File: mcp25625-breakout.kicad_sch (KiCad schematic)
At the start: 9 parts

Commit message: Apply KiCad6 lib
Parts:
- SW1: symbol my-kicad-symbols:SW_Slide_with_cover -> asukiaaa-kicad-symbols:SW_Slide_with_cover
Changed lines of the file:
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@@
     (pin "9")
   )
-  (symbol (lib_id "my-kicad-symbols:SW_Slide_with_cover") (at 168.91 63.5 0) (mirror y) (unit 1)
+  (symbol (lib_id "asukiaaa-kicad-symbols:SW_Slide_with_cover") (at 168.91 63.5 0) (mirror y) (unit 1)
     (in_bom yes) (on_board yes)
     (property "Reference" "SW1" (id 0) (at 168.91 56.261 0))
@@
     )
     (path "/00000000-0000-0000-0000-000060a42d68"
-      (reference "J1") (unit 1) (value "Conn_01x11") (footprint "my-kicad-footprints:PinHeader_1x11_P2.54mm_Vertical_witout_silk")
+      (reference "J1") (unit 1) (value "Conn_01x11") (footprint "asukiaaa-kicad-footprints:PinHeader_1x11_P2.54mm_Vertical_witout_silk")
     )
     (path "/00000000-0000-0000-0000-00006097b02f"
@@
     )
     (path "/00000000-0000-0000-0000-000060bd7c69"
-      (reference "SW1") (unit 1) (value "SW_Slide_with_cover") (footprint "my-kicad-footprints:slide_switch_smd")
+      (reference "SW1") (unit 1) (value "SW_Slide_with_cover") (footprint "asukiaaa-kicad-footprints:slide_switch_smd")
     )
     (path "/00000000-0000-0000-0000-000060968f8d"

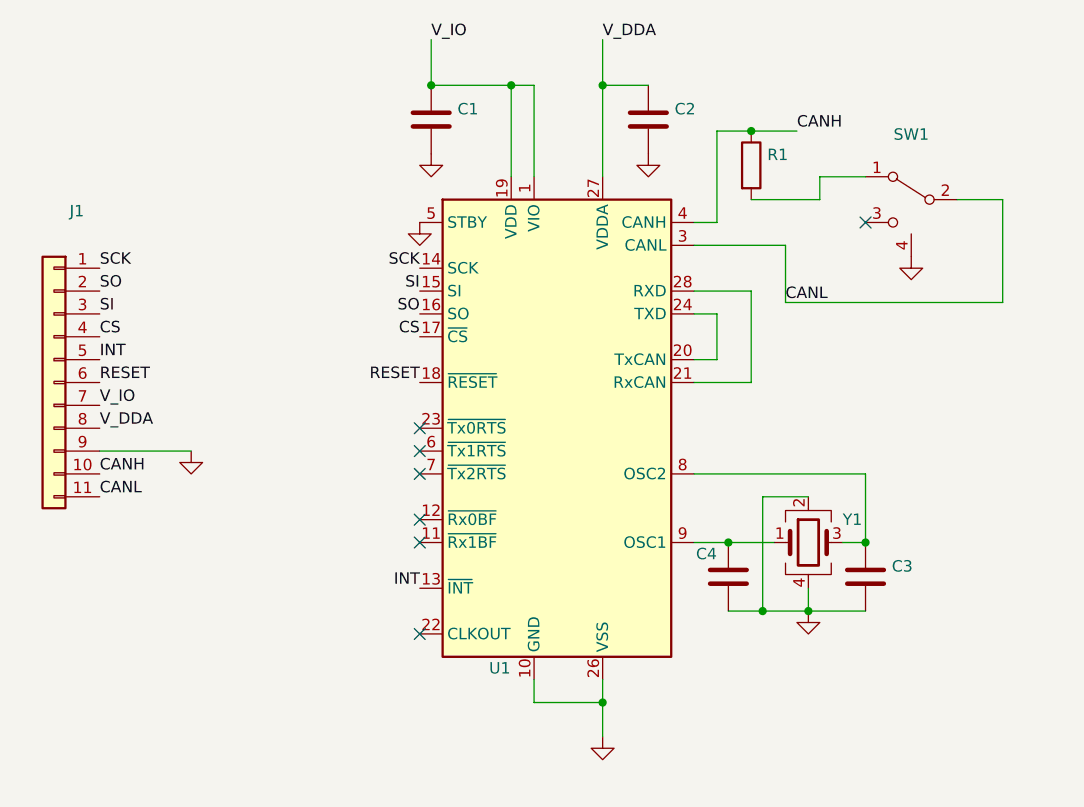
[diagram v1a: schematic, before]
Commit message: Change to not hand solder pad for crystal
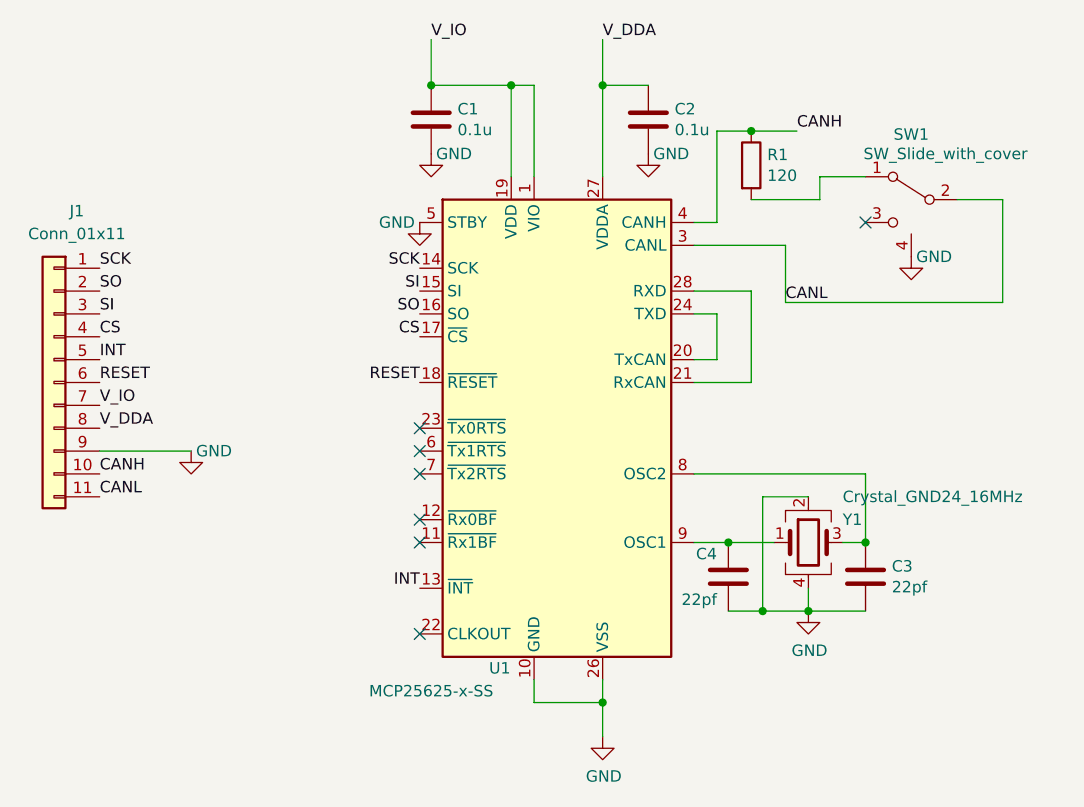
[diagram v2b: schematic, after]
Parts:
- C1, C2: value (none) -> 0.1u; footprint (none) -> Capacitor_SMD:C_0402_1005Metric
- C3, C4: value (none) -> 22pf; footprint (none) -> Capacitor_SMD:C_0402_1005Metric
- J1: value (none) -> Conn_01x11; footprint (none) -> asukiaaa-kicad-footprints:PinHeader_1x11_P2.54mm_Vertical_witout_silk
- R1: value (none) -> 120; footprint (none) -> Resistor_SMD:R_0402_1005Metric
- SW1: value (none) -> SW_Slide_with_cover; footprint (none) -> asukiaaa-kicad-footprints:slide_switch_smd
- U1: value (none) -> MCP25625-x-SS; footprint (none) -> Package_SO:SSOP-28_5.3x10.2mm_P0.65mm
- Y1: value (none) -> Crystal_GND24_16MHz; footprint (none) -> Crystal:Crystal_SMD_SeikoEpson_FA238-4Pin_3.2x2.5mm
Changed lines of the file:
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@@
     (in_bom yes) (on_board yes)
     (property "Reference" "U1" (id 0) (at 123.19 115.57 0))
-    (property "Value" "" (id 1) (at 115.57 118.11 0))
-    (property "Footprint" "" (id 2) (at 132.08 96.52 0)
+    (property "Value" "MCP25625-x-SS" (id 1) (at 115.57 118.11 0))
+    (property "Footprint" "Package_SO:SSOP-28_5.3x10.2mm_P0.65mm" (id 2) (at 132.08 96.52 0)
       (effects (font (size 1.27 1.27)) hide)
     )
@@
       (effects (font (size 1.27 1.27)) hide)
     )
-    (property "Value" "" (id 1) (at 134.747 127.5842 0))
+    (property "Value" "GND" (id 1) (at 134.747 127.5842 0))
     (property "Footprint" "" (id 2) (at 134.62 123.19 0)
       (effects (font (size 1.27 1.27)) hide)
@@
       (effects (font (size 1.27 1.27)) (justify left))
     )
-    (property "Value" "" (id 1) (at 142.621 55.753 0)
-      (effects (font (size 1.27 1.27)) (justify left))
-    )
-    (property "Footprint" "" (id 2) (at 140.6652 58.42 0)
+    (property "Value" "0.1u" (id 1) (at 142.621 55.753 0)
+      (effects (font (size 1.27 1.27)) (justify left))
+    )
+    (property "Footprint" "Capacitor_SMD:C_0402_1005Metric" (id 2) (at 140.6652 58.42 0)
       (effects (font (size 1.27 1.27)) hide)
     )
@@
       (effects (font (size 1.27 1.27)) (justify left))
     )
-    (property "Value" "" (id 1) (at 118.491 55.753 0)
-      (effects (font (size 1.27 1.27)) (justify left))
-    )
-    (property "Footprint" "" (id 2) (at 116.5352 58.42 0)
+    (property "Value" "0.1u" (id 1) (at 118.491 55.753 0)
+      (effects (font (size 1.27 1.27)) (justify left))
+    )
+    (property "Footprint" "Capacitor_SMD:C_0402_1005Metric" (id 2) (at 116.5352 58.42 0)
       (effects (font (size 1.27 1.27)) hide)
     )
@@
       (effects (font (size 1.27 1.27)) hide)
     )
-    (property "Value" "" (id 1) (at 142.24 58.42 0))
+    (property "Value" "GND" (id 1) (at 142.24 58.42 0))
     (property "Footprint" "" (id 2) (at 139.7 58.42 0)
       (effects (font (size 1.27 1.27)) hide)
@@
       (effects (font (size 1.27 1.27)) hide)
     )
-    (property "Value" "" (id 1) (at 111.76 66.04 0))
+    (property "Value" "GND" (id 1) (at 111.76 66.04 0))
     (property "Footprint" "" (id 2) (at 114.3 66.04 0)
       (effects (font (size 1.27 1.27)) hide)
@@
       (effects (font (size 1.27 1.27)) hide)
     )
-    (property "Value" "" (id 1) (at 118.11 58.42 0))
+    (property "Value" "GND" (id 1) (at 118.11 58.42 0))
     (property "Footprint" "" (id 2) (at 115.57 58.42 0)
       (effects (font (size 1.27 1.27)) hide)
@@
       (effects (font (size 1.27 1.27)) (justify left))
     )
-    (property "Value" "" (id 1) (at 152.908 60.833 0)
-      (effects (font (size 1.27 1.27)) (justify left))
-    )
-    (property "Footprint" "" (id 2) (at 149.352 59.69 90)
+    (property "Value" "120" (id 1) (at 152.908 60.833 0)
+      (effects (font (size 1.27 1.27)) (justify left))
+    )
+    (property "Footprint" "Resistor_SMD:R_0402_1005Metric" (id 2) (at 149.352 59.69 90)
       (effects (font (size 1.27 1.27)) hide)
     )
@@
       (effects (font (size 1.27 1.27)) hide)
     )
-    (property "Value" "" (id 1) (at 91.44 91.44 0))
+    (property "Value" "GND" (id 1) (at 91.44 91.44 0))
     (property "Footprint" "" (id 2) (at 88.9 91.44 0)
       (effects (font (size 1.27 1.27)) hide)
@@
     (in_bom yes) (on_board yes)
     (property "Reference" "J1" (id 0) (at 76.2 64.77 0))
-    (property "Value" "" (id 1) (at 76.2 67.31 0))
-    (property "Footprint" "" (id 2) (at 73.66 83.82 0)
+    (property "Value" "Conn_01x11" (id 1) (at 76.2 67.31 0))
+    (property "Footprint" "asukiaaa-kicad-footprints:PinHeader_1x11_P2.54mm_Vertical_witout_silk" (id 2) (at 73.66 83.82 0)
       (effects (font (size 1.27 1.27)) hide)
     )
@@
     (in_bom yes) (on_board yes)
     (property "Reference" "SW1" (id 0) (at 168.91 56.261 0))
-    (property "Value" "" (id 1) (at 172.72 58.42 0))
-    (property "Footprint" "" (id 2) (at 168.91 63.5 0)
+    (property "Value" "SW_Slide_with_cover" (id 1) (at 172.72 58.42 0))
+    (property "Footprint" "asukiaaa-kicad-footprints:slide_switch_smd" (id 2) (at 168.91 63.5 0)
       (effects (font (size 1.27 1.27)) hide)
     )
@@
       (effects (font (size 1.27 1.27)) hide)
     )
-    (property "Value" "" (id 1) (at 171.45 69.85 0))
+    (property "Value" "GND" (id 1) (at 171.45 69.85 0))
     (property "Footprint" "" (id 2) (at 168.91 69.85 0)
       (effects (font (size 1.27 1.27)) hide)
@@
       (effects (font (size 1.27 1.27)) (justify left))
     )
-    (property "Value" "" (id 1) (at 147.32 107.95 0)
-      (effects (font (size 1.27 1.27)) (justify left))
-    )
-    (property "Footprint" "" (id 2) (at 147.6248 109.22 0)
+    (property "Value" "22pf" (id 1) (at 147.32 107.95 0)
+      (effects (font (size 1.27 1.27)) (justify left))
+    )
+    (property "Footprint" "Capacitor_SMD:C_0402_1005Metric" (id 2) (at 147.6248 109.22 0)
       (effects (font (size 1.27 1.27)) hide)
     )
@@
       (effects (font (size 1.27 1.27)) (justify left))
     )
-    (property "Value" "" (id 1) (at 161.29 96.52 0)
-      (effects (font (size 1.27 1.27)) (justify left))
-    )
-    (property "Footprint" "" (id 2) (at 157.48 101.6 0)
+    (property "Value" "Crystal_GND24_16MHz" (id 1) (at 161.29 96.52 0)
+      (effects (font (size 1.27 1.27)) (justify left))
+    )
+    (property "Footprint" "Crystal:Crystal_SMD_SeikoEpson_FA238-4Pin_3.2x2.5mm" (id 2) (at 157.48 101.6 0)
       (effects (font (size 1.27 1.27)) hide)
     )
@@
       (effects (font (size 1.27 1.27)) (justify left))
     )
-    (property "Value" "" (id 1) (at 166.751 106.553 0)
-      (effects (font (size 1.27 1.27)) (justify left))
-    )
-    (property "Footprint" "" (id 2) (at 164.7952 109.22 0)
+    (property "Value" "22pf" (id 1) (at 166.751 106.553 0)
+      (effects (font (size 1.27 1.27)) (justify left))
+    )
+    (property "Footprint" "Capacitor_SMD:C_0402_1005Metric" (id 2) (at 164.7952 109.22 0)
       (effects (font (size 1.27 1.27)) hide)
     )
@@
       (effects (font (size 1.27 1.27)) hide)
     )
-    (property "Value" "" (id 1) (at 157.607 113.6142 0))
+    (property "Value" "GND" (id 1) (at 157.607 113.6142 0))
     (property "Footprint" "" (id 2) (at 157.48 109.22 0)
       (effects (font (size 1.27 1.27)) hide)
@@
     )
     (path "/00000000-0000-0000-0000-000061607a20"
-      (reference "Y1") (unit 1) (value "Crystal_GND24_16MHz") (footprint "Crystal:Crystal_SMD_SeikoEpson_FA238-4Pin_3.2x2.5mm_HandSoldering")
-    )
-  )
+      (reference "Y1") (unit 1) (value "Crystal_GND24_16MHz") (footprint "Crystal:Crystal_SMD_SeikoEpson_FA238-4Pin_3.2x2.5mm")
+    )
+  )

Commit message: Add resistor between rst and vio as rev2023.05
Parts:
- added R2: 10k, Resistor_SMD:R_0402_1005Metric, symbol Device:R
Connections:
- net RESET: now also R2.2
- net V_IO: now also R2.1
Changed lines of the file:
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@@
   (junction (at 163.83 101.6) (diameter 0) (color 0 0 0 0)
+  )
+  (junction (at 104.775 83.82) (diameter 0) (color 0 0 0 0)
   )
   (junction (at 124.46 50.8) (diameter 0) (color 0 0 0 0)
@@
     (stroke (width 0) (type default) (color 0 0 0 0))
   )
+  (wire (pts (xy 102.87 83.82) (xy 104.775 83.82))
+    (stroke (width 0) (type default) (color 0 0 0 0))
+  )
   (wire (pts (xy 152.4 96.52) (xy 152.4 109.22))
     (stroke (width 0) (type default) (color 0 0 0 0))
   )
+  (wire (pts (xy 104.775 83.82) (xy 114.3 83.82))
+    (stroke (width 0) (type default) (color 0 0 0 0))
+  )
   (wire (pts (xy 144.78 66.04) (xy 147.32 66.04))
     (stroke (width 0) (type default) (color 0 0 0 0))
@@
     (effects (font (size 1.27 1.27)) (justify right bottom))
   )
-  (label "RESET" (at 114.3 83.82 180)
+  (label "RESET" (at 102.87 83.82 180)
     (effects (font (size 1.27 1.27)) (justify right bottom))
   )
@@
   (label "SI" (at 78.74 76.2 0)
     (effects (font (size 1.27 1.27)) (justify left bottom))
+  )
+  (label "V_IO" (at 104.775 76.2 180)
+    (effects (font (size 1.27 1.27)) (justify right bottom))
   )
   (label "CANL" (at 78.74 96.52 0)
@@
     (pin "1")
   )
+  (symbol (lib_id "Device:R") (at 104.775 80.01 0) (unit 1)
+    (in_bom yes) (on_board yes)
+    (property "Reference" "R2" (id 0) (at 106.553 78.8416 0)
+      (effects (font (size 1.27 1.27)) (justify left))
+    )
+    (property "Value" "10k" (id 1) (at 106.553 81.153 0)
+      (effects (font (size 1.27 1.27)) (justify left))
+    )
+    (property "Footprint" "Resistor_SMD:R_0402_1005Metric" (id 2) (at 102.997 80.01 90)
+      (effects (font (size 1.27 1.27)) hide)
+    )
+    (property "Datasheet" "~" (id 3) (at 104.775 80.01 0)
+      (effects (font (size 1.27 1.27)) hide)
+    )
+    (pin "1")
+    (pin "2")
+  )
   (sheet_instances
     (path "/" (page "1"))
@@
       (reference "R1") (unit 1) (value "120") (footprint "Resistor_SMD:R_0402_1005Metric")
     )
+    (path "/9647d562-480a-47c5-9f61-5965f7e73b4a"
+      (reference "R2") (unit 1) (value "10k") (footprint "Resistor_SMD:R_0402_1005Metric")
+    )
     (path "/00000000-0000-0000-0000-000060bd7c69"
